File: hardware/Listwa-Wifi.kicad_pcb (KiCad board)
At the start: 2 copper layers, 88.3 x 29.2 mm, 34 parts, among them J1 230-VAC-L, J2 230-VAC-OUT, J3 Prog-Power, J4 230-VAC-N, J5 PROG-Data, SW1 RESET, SW2 BOOT, U1 AMEOF3-JZ, U2 G5RL-K1A-E-5DC, U3 ESP-12E, U4 NX7002AK.215, U5 NX7002AK.215

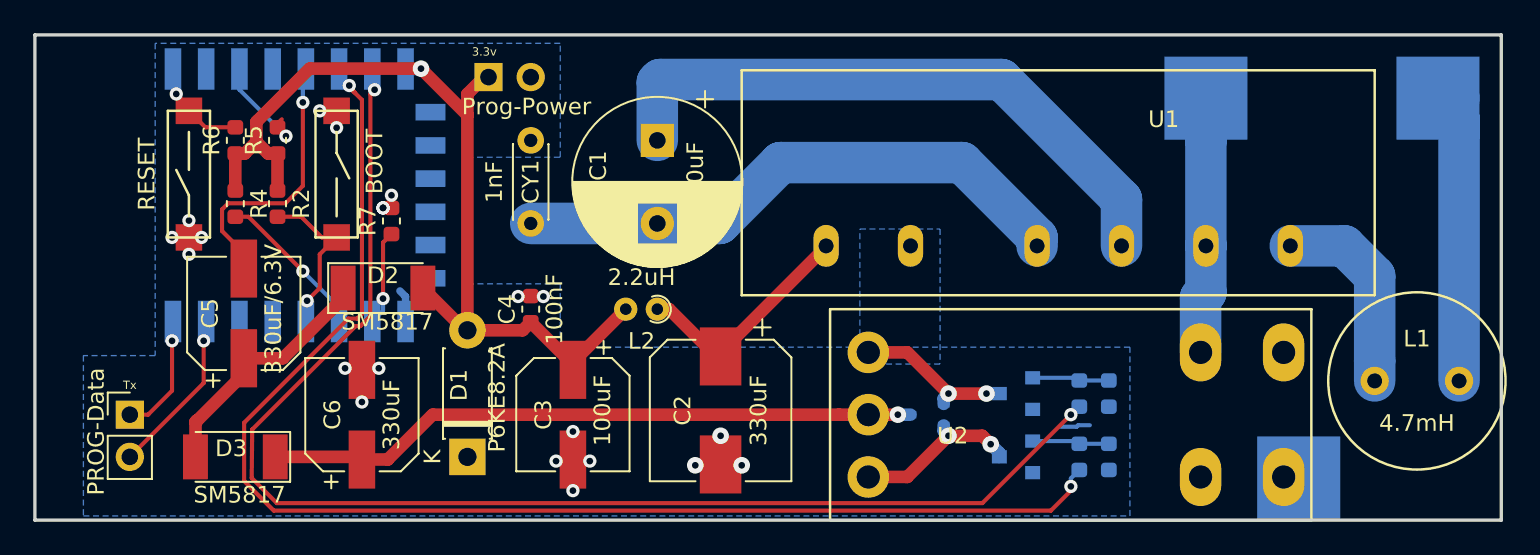
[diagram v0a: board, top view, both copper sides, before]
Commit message: Add holes on pads, better GND plane
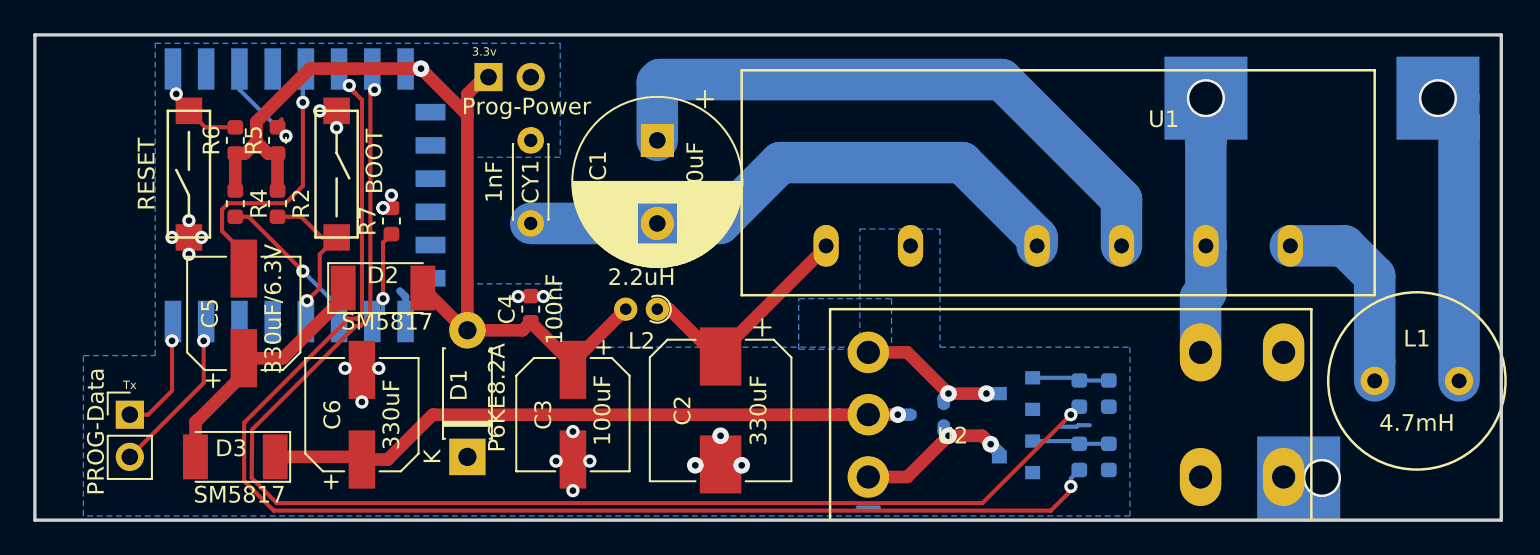
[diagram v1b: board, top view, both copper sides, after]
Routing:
- net (no net): track 1.85 -> 3.12 mm
- net Net-(J4-Pad1): vias 0 -> 1
- net Net-(J2-Pad1): vias 0 -> 1
- net 230-VAC-L: vias 0 -> 1
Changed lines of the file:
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@@
     (thickness 1.6)
     (drawings 6)
-    (tracks 221)
+    (tracks 227)
     (zones 0)
     (modules 34)
@@
       (padsonsilk false)
       (subtractmaskfromsilk false)
-      (outputformat 1)
+      (outputformat 4)
       (mirror false)
-      (drillshape 1)
+      (drillshape 0)
       (scaleselection 1)
-      (outputdirectory ""))
+      (outputdirectory "../../../Desktop/pcb"))
   )
   (net 0 "")
@@
   (segment (start 120.65 106.68) (end 119.945002 106.68) (width 0.25) (layer B.Cu) (net 0))
   (segment (start 119.945002 106.68) (end 119.855001 106.770001) (width 0.25) (layer B.Cu) (net 0))
-  (via (at 67.183 95.377) (size 0.8) (drill 0.4) (layers F.Cu B.Cu) (net 35))
-  (via (at 89.535 107.061) (size 0.8) (drill 0.4) (layers F.Cu B.Cu) (net 35))
-  (via (at 98.425 107.315) (size 1) (drill 0.4) (layers F.Cu B.Cu) (net 35))
-  (via (at 72.263 89.281) (size 0.8) (drill 0.4) (layers F.Cu B.Cu) (net 17))
-  (via (at 73.533 99.187) (size 0.8) (drill 0.4) (layers F.Cu B.Cu) (net 29))
-  (via (at 65.659 86.741) (size 0.8) (drill 0.4) (layers F.Cu B.Cu) (net 16))
+  (segment (start 106.68 111.633) (end 107.95 111.633) (width 0.25) (layer B.Cu) (net 0))
+  (via (at 134.62 109.855) (size 2.3) (drill 2) (layers F.Cu B.Cu) (net 8))
   (segment (start 89.535 102.875) (end 92.715 99.695) (width 0.76) (layer F.Cu) (net 1))
   (segment (start 89.535 103.345) (end 89.535 102.875) (width 0.76) (layer F.Cu) (net 1))
@@
   (segment (start 111.855 106.695) (end 111.855 107.029) (width 0.76) (layer B.Cu) (net 6))
   (segment (start 127.635 95.885) (end 127.635 89.55001) (width 2.5) (layer B.Cu) (net 7))
-  (segment (start 127.635 86.995) (end 127.635 89.55001) (width 2.5) (layer B.Cu) (net 7))
+  (segment (start 127.635 86.995) (end 127.635 86.995) (width 2.5) (layer B.Cu) (net 7))
   (segment (start 127.315 102.295) (end 127.315 98.999) (width 2.5) (layer B.Cu) (net 7))
   (segment (start 127.635 98.679) (end 127.635 95.885) (width 2.5) (layer B.Cu) (net 7))
   (segment (start 127.315 98.999) (end 127.635 98.679) (width 2.5) (layer B.Cu) (net 7))
+  (segment (start 127.635 86.995) (end 127.635 89.55001) (width 2.5) (layer B.Cu) (net 7))
+  (via (at 127.635 86.995) (size 2.3) (drill 2) (layers F.Cu B.Cu) (net 7))
   (segment (start 132.375 109.855) (end 132.315 109.795) (width 2.5) (layer B.Cu) (net 8))
   (segment (start 62.865 108.585) (end 67.31 104.14) (width 0.25) (layer F.Cu) (net 9))
@@
   (segment (start 65.405 104.605) (end 65.405 101.6) (width 0.25) (layer F.Cu) (net 10))
   (via (at 65.405 101.6) (size 0.8) (drill 0.4) (layers F.Cu B.Cu) (net 10))
-  (segment (start 141.605 86.995) (end 142.875 86.995) (width 2.5) (layer B.Cu) (net 11))
+  (segment (start 141.605 86.995) (end 141.605 86.995) (width 2.5) (layer B.Cu) (net 11))
   (segment (start 142.875 88.265) (end 141.605 86.995) (width 2.5) (layer B.Cu) (net 11))
   (segment (start 142.875 104.013) (end 142.875 88.265) (width 2.5) (layer B.Cu) (net 11))
+  (segment (start 141.605 86.995) (end 142.875 86.995) (width 2.5) (layer B.Cu) (net 11))
+  (via (at 141.605 86.995) (size 2.3) (drill 2) (layers F.Cu B.Cu) (net 11))
   (segment (start 137.795 97.703) (end 137.795 102.810919) (width 2.5) (layer B.Cu) (net 12))
   (segment (start 135.977 95.885) (end 137.795 97.703) (width 2.5) (layer B.Cu) (net 12))
@@
   (segment (start 95.325 99.695) (end 98.425 102.795) (width 0.76) (layer F.Cu) (net 15))
   (segment (start 98.425 102.295) (end 104.775 95.945) (width 0.76) (layer F.Cu) (net 15))
+  (via (at 65.659 86.741) (size 0.8) (drill 0.4) (layers F.Cu B.Cu) (net 16))
   (segment (start 67.4115 88.7475) (end 66.421 87.757) (width 0.25) (layer F.Cu) (net 16))
   (segment (start 69.215 88.7475) (end 67.4115 88.7475) (width 0.25) (layer F.Cu) (net 16))
@@
   (segment (start 65.461 86.543) (end 65.659 86.741) (width 0.25) (layer B.Cu) (net 16))
   (segment (start 65.461 85.237) (end 65.461 86.543) (width 0.25) (layer B.Cu) (net 16))
+  (via (at 72.263 89.281) (size 0.8) (drill 0.4) (layers F.Cu B.Cu) (net 17))
   (segment (start 71.755 88.519) (end 72.009 88.265) (width 0.25) (layer F.Cu) (net 17))
   (segment (start 71.755 88.7475) (end 71.755 88.519) (width 0.25) (layer F.Cu) (net 17))
@@
   (segment (start 75.461 99.591) (end 75.461 100.437) (width 0.25) (layer B.Cu) (net 28))
   (segment (start 73.279 97.409) (end 75.461 99.591) (width 0.25) (layer B.Cu) (net 28))
+  (via (at 73.533 99.187) (size 0.8) (drill 0.4) (layers F.Cu B.Cu) (net 29))
   (segment (start 74.422 95.377) (end 75.311 95.377) (width 0.25) (layer F.Cu) (net 29))
   (segment (start 71.755 94.1325) (end 73.1775 94.1325) (width 0.25) (layer F.Cu) (net 29))
@@
   (segment (start 117.205 107.635) (end 119.8525 107.635) (width 0.25) (layer B.Cu) (net 33))
   (segment (start 120.015 107.7975) (end 121.793 107.7975) (width 0.25) (layer B.Cu) (net 33))
+  (via (at 67.183 95.377) (size 0.8) (drill 0.4) (layers F.Cu B.Cu) (net 35))
+  (via (at 89.535 107.061) (size 0.8) (drill 0.4) (layers F.Cu B.Cu) (net 35))
+  (via (at 98.425 107.315) (size 1) (drill 0.4) (layers F.Cu B.Cu) (net 35))
   (via (at 96.901 109.093) (size 1) (drill 0.4) (layers F.Cu B.Cu) (net 35))
   (via (at 99.695 109.093) (size 1) (drill 0.4) (layers F.Cu B.Cu) (net 35))
@@
   (segment (start 99.643 109.041) (end 99.695 109.093) (width 0.25) (layer F.Cu) (net 35))
   (segment (start 98.425 109.041) (end 99.643 109.041) (width 0.25) (layer F.Cu) (net 35))
-  (segment (start 98.425 109.041) (end 98.425 107.315) (width 0.25) (layer F.Cu) (net 35))
   (via (at 88.519 108.839) (size 0.8) (drill 0.4) (layers F.Cu B.Cu) (net 35))
   (via (at 90.551 108.839) (size 0.8) (drill 0.4) (layers F.Cu B.Cu) (net 35))
@@
   (segment (start 79.461 98.937) (end 79.121 98.597) (width 0.45) (layer B.Cu) (net 35))
   (segment (start 79.461 100.437) (end 79.461 98.937) (width 0.45) (layer B.Cu) (net 35))
+  (segment (start 98.425 109.041) (end 98.425 107.315) (width 0.25) (layer F.Cu) (net 35))
   (zone (net 35) (net_name Earth) (layer B.Cu) (hatch edge 0.508)
     (connect_pads (clearance 0.508))
@@
     (polygon
       (pts
-        (xy 64.389 83.693) (xy 64.389 102.489) (xy 60.071 102.489) (xy 60.071 112.141) (xy 123.063 112.141)
-        (xy 123.063 101.981) (xy 88.773 101.981) (xy 88.773 98.171) (xy 83.185 98.171) (xy 83.185 90.551)
-        (xy 88.773 90.551) (xy 88.773 83.693)
+        (xy 88.773 90.551) (xy 83.185 90.551) (xy 83.185 98.171) (xy 88.773 98.171) (xy 88.773 101.981)
+        (xy 106.807 101.981) (xy 106.807 94.869) (xy 111.633 94.869) (xy 111.633 101.981) (xy 123.063 101.981)
+        (xy 123.063 112.141) (xy 60.071 112.141) (xy 60.071 102.489) (xy 64.389 102.489) (xy 64.389 83.693)
+        (xy 88.773 83.693)
       )
     )
@@
     (polygon
       (pts
-        (xy 106.807 102.997) (xy 106.807 94.869) (xy 111.633 94.869) (xy 111.633 102.997)
+        (xy 103.124 102.108) (xy 103.124 99.06) (xy 108.712 99.06) (xy 108.712 102.108)
       )
     )
